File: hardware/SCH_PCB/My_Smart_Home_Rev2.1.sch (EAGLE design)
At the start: 88 parts, among them J1 ISP0, J2 ISP1, J3 MICROUSB-5P, J4 JUMPER, J5 13F-60FGYDPNW2NL, Q1 CJ2302, SW2 SW-2, U1 ATMEGA8U2, U2 ATMEGAXX8-AU, U3 W5100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

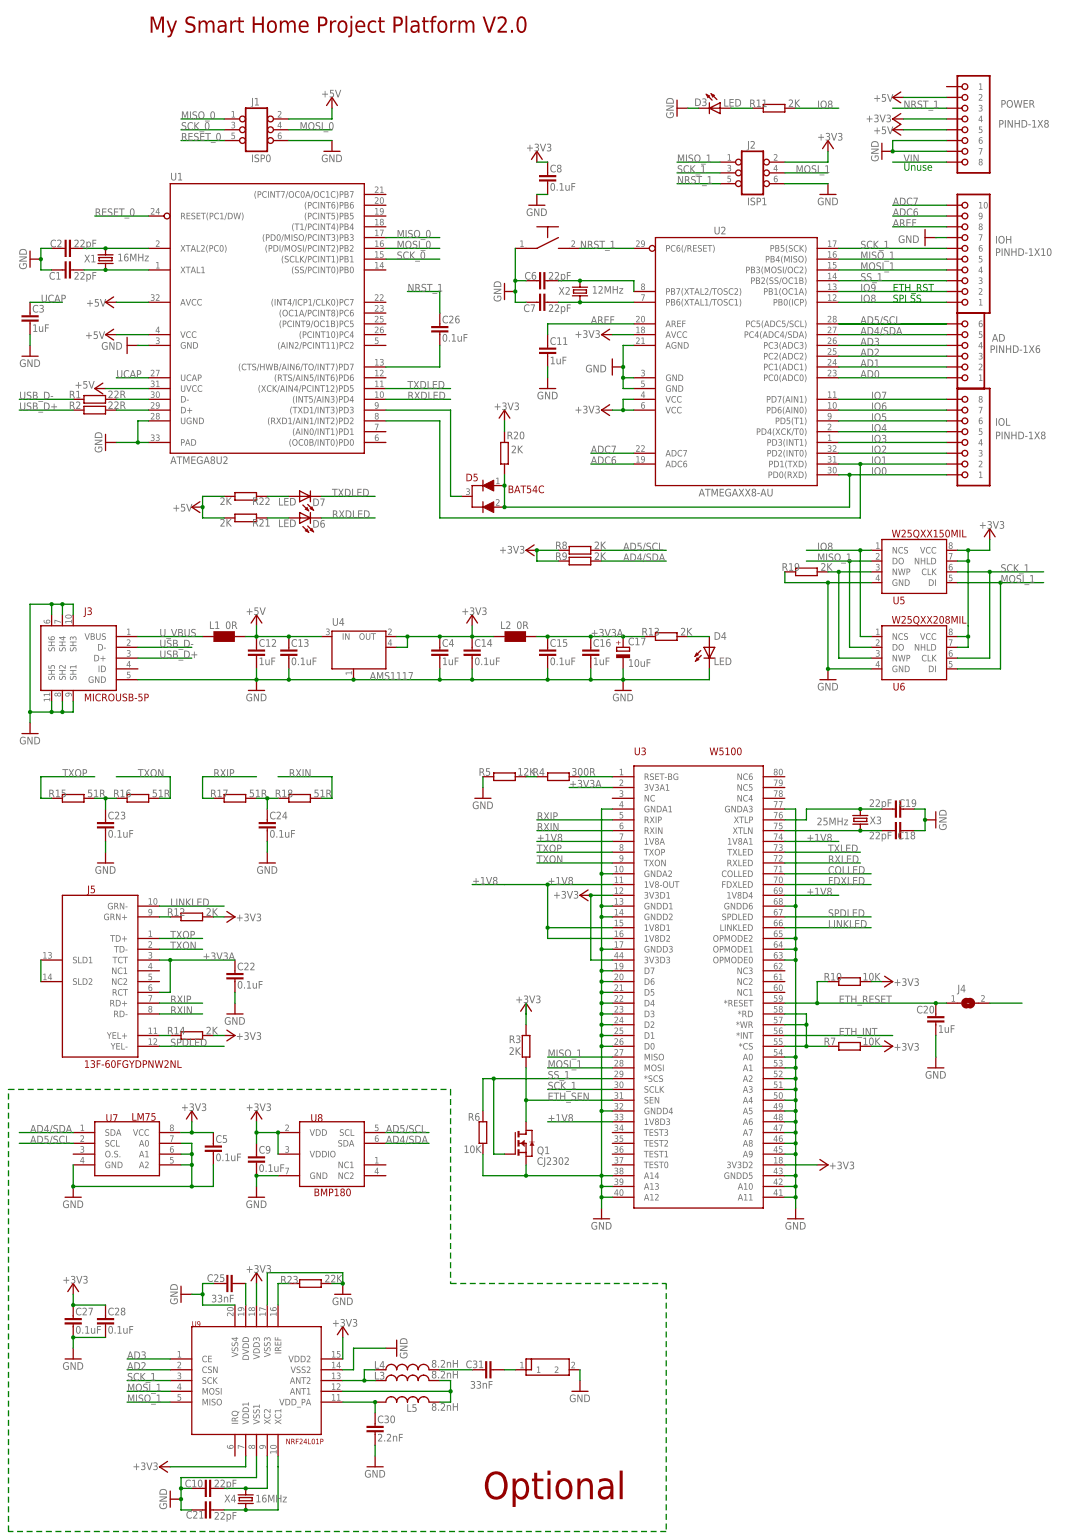
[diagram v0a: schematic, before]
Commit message: Fix Hellduino V2.0 HW bugs, HW version update to V2.1
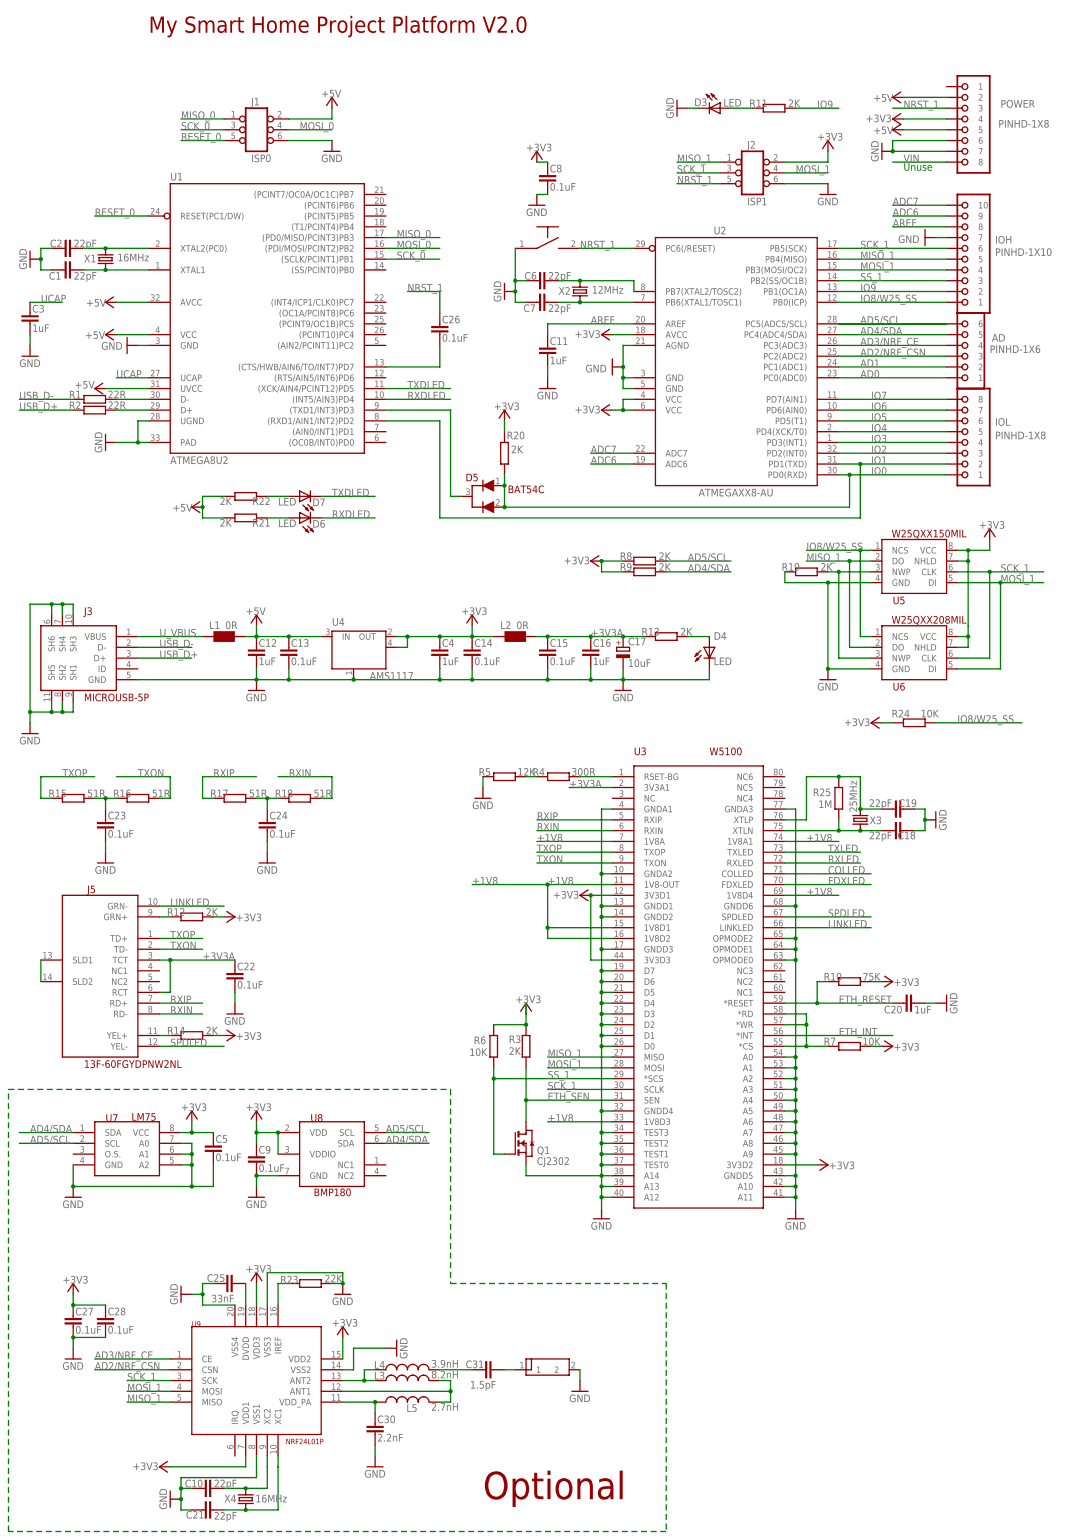
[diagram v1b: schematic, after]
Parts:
- removed J4: JUMPER, Hell-Prototypes:JUMPER
- added R24: 10K, Hell-Prototypes:RES
- added R25: 1M, Hell-Prototypes:RES
- C31: value 33nF -> 1.5pF
- L4: value 8.2nH -> 3.9nH
- L5: value 8.2nH -> 2.7nH
- R10: value 10K -> 75K
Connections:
- net AD2 renamed AD2/NRF_CSN
- net AD3 renamed AD3/NRF_CE
- removed net IO8: IOH.1, R11.1, U2.PB0(ICP), U5.NCS, U6.NCS
- new net IO8/W25_SS: IOH.1, R24.2, U2.PB0(ICP), U5.NCS, U6.NCS
- net +3V3: now also R24.1, R6.1
- net ETH_RESET: no longer J4.1
- net GND: now also U3.TEST0, U3.TEST1, U3.TEST2, U3.TEST3; no longer R6.1
- net IO9: now also R11.1; no longer J4.2
- net N$3: now also R25.2
- net N$5: now also R25.1
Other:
- note removed: "ETH_RST"
- note removed: "SPI SS"
- moved on the sheet: C20, R6, R8, R9
